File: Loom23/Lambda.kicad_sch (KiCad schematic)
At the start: 0 parts

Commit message: Signed-off-by: fst29 <fst29@cam.ac.uk>
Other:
- note added: "Lambda controller"
- note added: "Lambda sensor"
- note added: "This might need to be sensor ground. Check documentation of sensor!"
- note added: "This whole sheet needs to be checked."
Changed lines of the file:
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@@
 (kicad_sch (version 20211123) (generator eeschema)
   (paper "A4")
+  (polyline (pts (xy 97.79 115.57) (xy 64.77 115.57))
+    (stroke (width 0) (type default) (color 0 0 0 0))
+  )
+  (polyline (pts (xy 64.77 99.06) (xy 64.77 115.57))
+    (stroke (width 0) (type default) (color 0 0 0 0))
+  )
+  (wire (pts (xy 148.59 110.49) (xy 160.02 110.49))
+    (stroke (width 0) (type default) (color 0 0 0 0))
+  )
+  (polyline (pts (xy 64.77 99.06) (xy 97.79 99.06))
+    (stroke (width 0) (type default) (color 0 0 0 0))
+  )
+  (polyline (pts (xy 121.92 118.11) (xy 121.92 100.33))
+    (stroke (width 0) (type default) (color 0 0 0 0))
+  )
+  (polyline (pts (xy 121.92 100.33) (xy 148.59 100.33))
+    (stroke (width 0) (type default) (color 0 0 0 0))
+  )
+  (bus (pts (xy 97.79 106.68) (xy 121.92 106.68))
+    (stroke (width 0) (type default) (color 0 0 0 0))
+  )
+  (polyline (pts (xy 148.59 118.11) (xy 121.92 118.11))
+    (stroke (width 0) (type default) (color 0 0 0 0))
+  )
+  (polyline (pts (xy 120.65 100.33) (xy 121.92 100.33))
+    (stroke (width 0) (type default) (color 0 0 0 0))
+  )
+  (polyline (pts (xy 148.59 100.33) (xy 148.59 118.11))
+    (stroke (width 0) (type default) (color 0 0 0 0))
+  )
+  (wire (pts (xy 148.59 106.68) (xy 160.02 106.68))
+    (stroke (width 0) (type default) (color 0 0 0 0))
+  )
+  (polyline (pts (xy 97.79 99.06) (xy 97.79 115.57))
+    (stroke (width 0) (type default) (color 0 0 0 0))
+  )
+  (wire (pts (xy 148.59 102.87) (xy 160.02 102.87))
+    (stroke (width 0) (type default) (color 0 0 0 0))
+  )
+  (text "This whole sheet needs to be checked." (at 29.21 34.29 0)
+    (effects (font (size 7 7)) (justify left bottom))
+  )
+  (text "Lambda sensor" (at 72.39 106.68 0)
+    (effects (font (size 1.27 1.27)) (justify left bottom))
+  )
+  (text "Lambda controller" (at 127 106.68 0)
+    (effects (font (size 1.27 1.27)) (justify left bottom))
+  )
+  (text "This might need to be sensor ground. Check documentation of sensor!"
+    (at 167.64 111.76 0)
+    (effects (font (size 1.27 1.27)) (justify left bottom))
+  )
+  (hierarchical_label "O2SIG" (shape input) (at 160.02 106.68 0)
+    (effects (font (size 1.27 1.27)) (justify left))
+  )
+  (hierarchical_label "GND" (shape input) (at 160.02 110.49 0)
+    (effects (font (size 1.27 1.27)) (justify left))
+  )
+  (hierarchical_label "+12V" (shape input) (at 160.02 102.87 0)
+    (effects (font (size 1.27 1.27)) (justify left))
+  )
 )

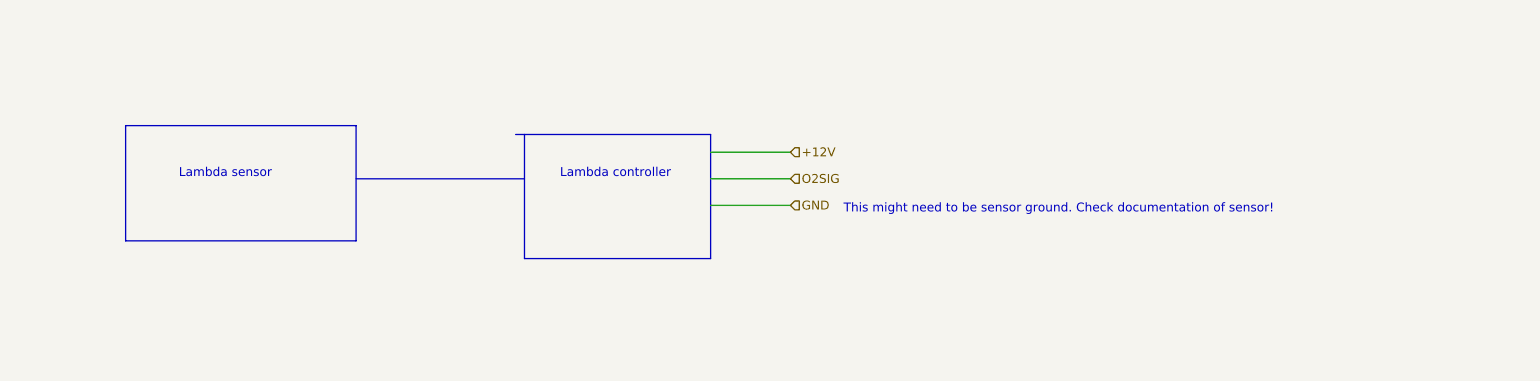
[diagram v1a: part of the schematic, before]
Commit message: Added fuel pump, TPS(BSPD), BPS.
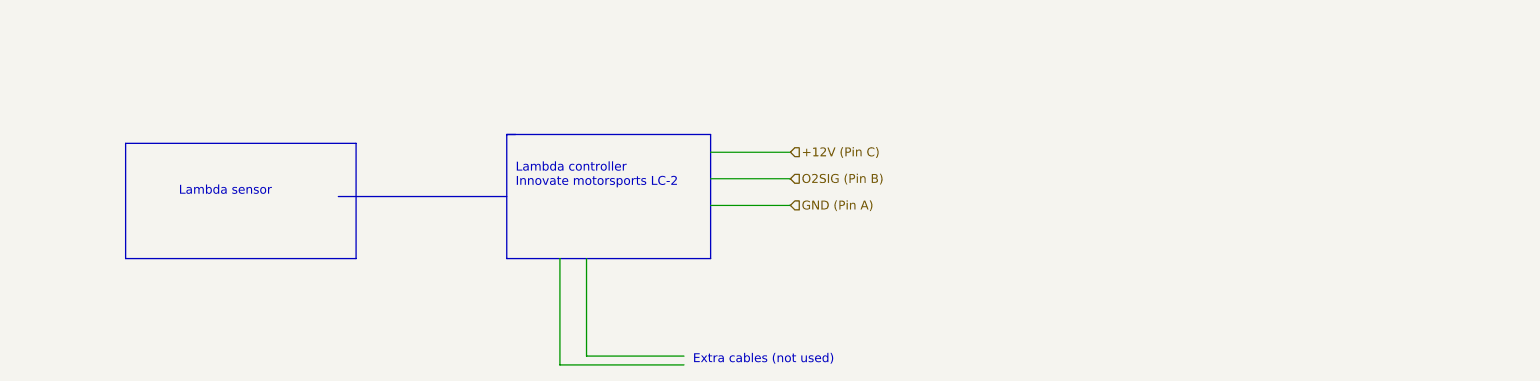
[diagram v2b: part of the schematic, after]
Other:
- note added: "Extra cables (not used)"
- note added: "Lambda controller Innovate motorsports LC-2"
- note removed: "Lambda controller"
- note removed: "This might need to be sensor ground. Check documentation of sensor!"
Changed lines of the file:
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@@
 (kicad_sch (version 20211123) (generator eeschema)
   (paper "A4")
-  (polyline (pts (xy 97.79 115.57) (xy 64.77 115.57))
+  (polyline (pts (xy 97.79 118.11) (xy 64.77 118.11))
     (stroke (width 0) (type default) (color 0 0 0 0))
   )
-  (polyline (pts (xy 64.77 99.06) (xy 64.77 115.57))
+  (polyline (pts (xy 64.77 101.6) (xy 64.77 118.11))
+    (stroke (width 0) (type default) (color 0 0 0 0))
+  )
+  (wire (pts (xy 127 133.35) (xy 144.78 133.35))
     (stroke (width 0) (type default) (color 0 0 0 0))
   )
@@
     (stroke (width 0) (type default) (color 0 0 0 0))
   )
-  (polyline (pts (xy 64.77 99.06) (xy 97.79 99.06))
+  (polyline (pts (xy 64.77 101.6) (xy 97.79 101.6))
     (stroke (width 0) (type default) (color 0 0 0 0))
   )
-  (polyline (pts (xy 121.92 118.11) (xy 121.92 100.33))
+  (polyline (pts (xy 119.38 118.11) (xy 119.38 100.33))
     (stroke (width 0) (type default) (color 0 0 0 0))
   )
-  (polyline (pts (xy 121.92 100.33) (xy 148.59 100.33))
+  (wire (pts (xy 130.81 118.11) (xy 130.81 132.08))
     (stroke (width 0) (type default) (color 0 0 0 0))
   )
-  (bus (pts (xy 97.79 106.68) (xy 121.92 106.68))
+  (polyline (pts (xy 119.38 100.33) (xy 148.59 100.33))
     (stroke (width 0) (type default) (color 0 0 0 0))
   )
-  (polyline (pts (xy 148.59 118.11) (xy 121.92 118.11))
+  (wire (pts (xy 130.81 132.08) (xy 144.78 132.08))
     (stroke (width 0) (type default) (color 0 0 0 0))
   )
-  (polyline (pts (xy 120.65 100.33) (xy 121.92 100.33))
+  (bus (pts (xy 95.25 109.22) (xy 119.38 109.22))
+    (stroke (width 0) (type default) (color 0 0 0 0))
+  )
+  (polyline (pts (xy 148.59 118.11) (xy 119.38 118.11))
+    (stroke (width 0) (type default) (color 0 0 0 0))
+  )
+  (wire (pts (xy 127 118.11) (xy 127 133.35))
+    (stroke (width 0) (type default) (color 0 0 0 0))
+  )
+  (polyline (pts (xy 120.65 100.33) (xy 119.38 100.33))
     (stroke (width 0) (type default) (color 0 0 0 0))
   )
@@
     (stroke (width 0) (type default) (color 0 0 0 0))
   )
-  (polyline (pts (xy 97.79 99.06) (xy 97.79 115.57))
+  (polyline (pts (xy 97.79 101.6) (xy 97.79 118.11))
     (stroke (width 0) (type default) (color 0 0 0 0))
   )
@@
     (stroke (width 0) (type default) (color 0 0 0 0))
   )
+  (text "Extra cables (not used)\n" (at 146.05 133.35 0)
+    (effects (font (size 1.27 1.27)) (justify left bottom))
+  )
   (text "This whole sheet needs to be checked." (at 29.21 34.29 0)
     (effects (font (size 7 7)) (justify left bottom))
   )
-  (text "Lambda sensor" (at 72.39 106.68 0)
+  (text "Lambda sensor" (at 72.39 109.22 0)
     (effects (font (size 1.27 1.27)) (justify left bottom))
   )
-  (text "Lambda controller" (at 127 106.68 0)
+  (text "Lambda controller\nInnovate motorsports LC-2" (at 120.65 107.95 0)
     (effects (font (size 1.27 1.27)) (justify left bottom))
   )
-  (text "This might need to be sensor ground. Check documentation of sensor!"
-    (at 167.64 111.76 0)
-    (effects (font (size 1.27 1.27)) (justify left bottom))
-  )
-  (hierarchical_label "O2SIG" (shape input) (at 160.02 106.68 0)
+  (hierarchical_label "O2SIG (Pin B)" (shape input) (at 160.02 106.68 0)
     (effects (font (size 1.27 1.27)) (justify left))
   )
-  (hierarchical_label "GND" (shape input) (at 160.02 110.49 0)
+  (hierarchical_label "GND (Pin A)" (shape input) (at 160.02 110.49 0)
     (effects (font (size 1.27 1.27)) (justify left))
   )
-  (hierarchical_label "+12V" (shape input) (at 160.02 102.87 0)
+  (hierarchical_label "+12V (Pin  C)" (shape input) (at 160.02 102.87 0)
     (effects (font (size 1.27 1.27)) (justify left))
   )

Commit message: Finished wiring up the ECU.
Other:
- note added: "Do NOT connect the LAMBDA GND to the Sensor ground of the ECU, this is a high current ground!"
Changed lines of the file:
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@@
+    (effects (font (size 1.27 1.27)) (justify left bottom))
+  )
+  (text "Do NOT connect the LAMBDA GND to the Sensor ground of the ECU, this is a high current ground!"
+    (at 177.8 111.76 0)
     (effects (font (size 1.27 1.27)) (justify left bottom))
   )
